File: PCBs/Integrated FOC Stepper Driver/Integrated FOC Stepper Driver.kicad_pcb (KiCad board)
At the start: 6 copper layers, 42 x 42 mm, 63 parts, among them J1 INPUT, J2 USB C Receptacle, J3 OUTPUT, J4 MOTOR, J5 Conn_01x02, SW1 BOOT, SW2 RESET, U1 PJ54M50SE, U2 PJ9500M33SA, U3 RP2040, U4 W25Q128JVS, U5 SN65HVD1050D, U6 MT6701CT, Y1 12MHz/12pF/50Ω/20ppm

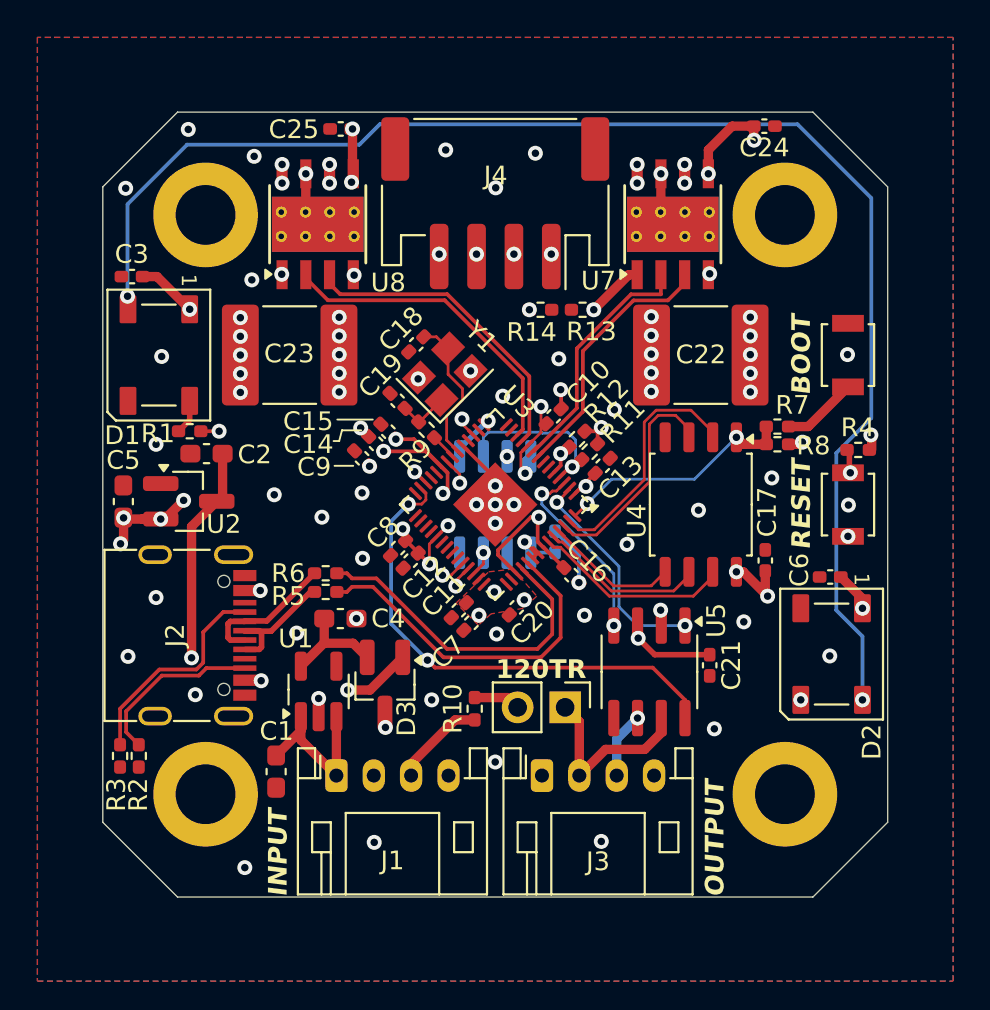
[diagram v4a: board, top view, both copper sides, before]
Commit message: Layout V2
Added a voltage divider from VBUS to measure up to 48V on ADC
Switch motor connector to JST-XH at 3A instead of 2A
Relayout to accomodate changes
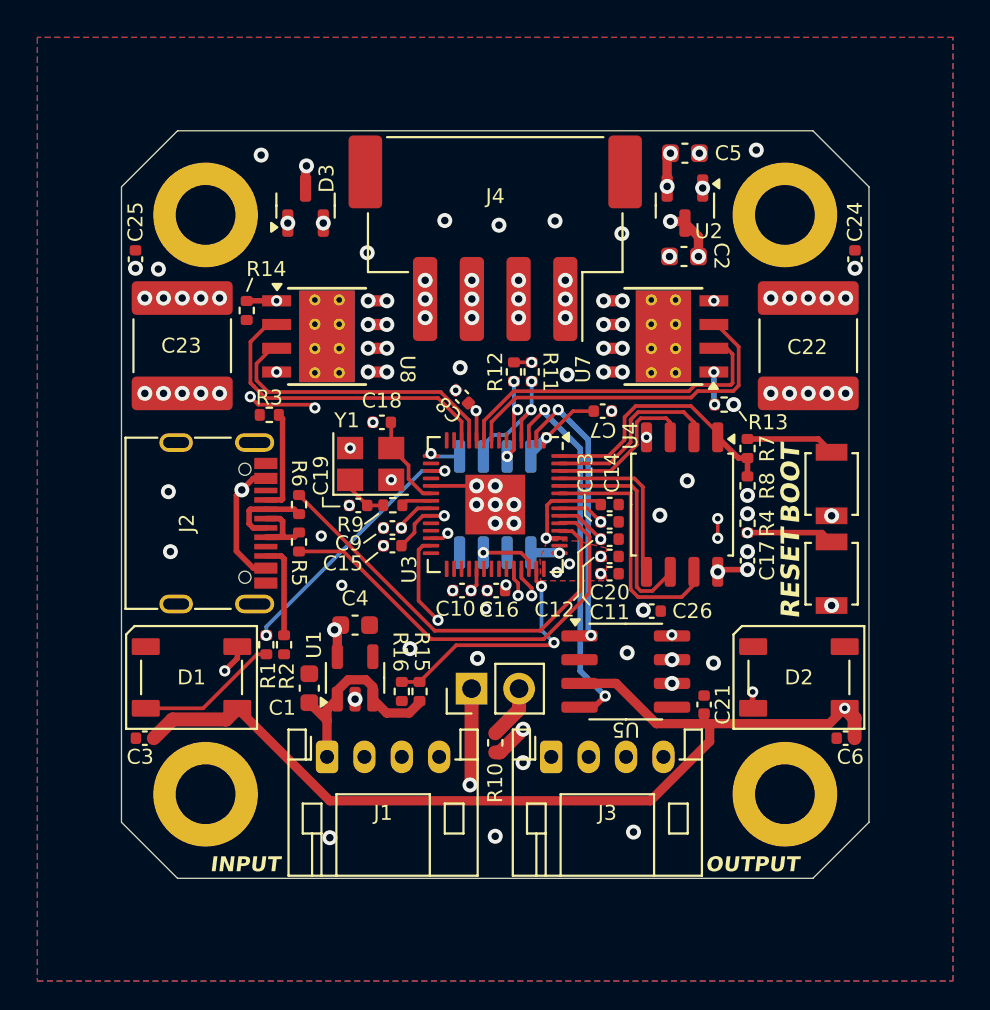
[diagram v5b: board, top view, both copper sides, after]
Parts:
- added R15: 150k, Resistor_SMD:R_0402_1005Metric, F.Cu at (46.0, 60.0)
- added R16: 10k, Resistor_SMD:R_0402_1005Metric, F.Cu at (45.0, 60.0)
- C1, C2, C4, C5: footprint Capacitor_SMD:C_0603_1608Metric_Pad1.08x0.95mm_HandSolder -> Capacitor_SMD:C_0603_1608Metric
- C10, C11, C12, C13, C14, C15, C16, C17, C18, C19, C20, C21, C24, C25, C3, C6, C7, C8, C9: footprint Capacitor_SMD:C_0402_1005Metric_Pad0.74x0.62mm_HandSolder -> Capacitor_SMD:C_0402_1005Metric
- C22, C23: footprint Capacitor_SMD:C_2220_5750Metric_Pad1.97x5.40mm_HandSolder -> Capacitor_SMD:C_2220_5750Metric
- C26: footprint Capacitor_SMD:C_0402_1005Metric_Pad0.74x0.62mm_HandSolder -> Capacitor_SMD:C_0402_1005Metric; moved to F.Cu
- D3, U2: footprint Package_TO_SOT_SMD:SOT-23_Handsoldering -> Package_TO_SOT_SMD:SOT-23
- J4: footprint Connector_JST:JST_PH_S4B-PH-SM4-TB_1x04-1MP_P2.00mm_Horizontal -> Connector_JST:JST_XH_S4B-XH-SM4-TB_1x04-1MP_P2.50mm_Horizontal
- R1, R10, R11, R12, R13, R14, R2, R3, R4, R5, R6, R7, R8, R9: footprint Resistor_SMD:R_0402_1005Metric_Pad0.72x0.64mm_HandSolder -> Resistor_SMD:R_0402_1005Metric
- U1: footprint Package_TO_SOT_SMD:SOT-23-5_HandSoldering -> Package_TO_SOT_SMD:SOT-23-5
- moved C5 35.4 mm to (60.1, 31.2), turned to 0 degrees
- moved U2 30.9 mm to (60.1, 34.0), turned to -90 degrees
- moved C2 27.6 mm to (60.1, 36.7)
- moved D3 26.0 mm to (39.9, 34.0), turned to 90 degrees
- moved C3 24.7 mm to (31.2, 62.5)
- moved R3 19.9 mm to (37.9, 45.2), turned to 180 degrees
- moved D1 17.3 mm to (33.8, 59.2), turned to 180 degrees
- moved R14 15.7 mm to (36.7, 39.6), turned to -90 degrees
- moved C7 13.3 mm to (55.8, 45.0), turned to 180 degrees
- moved C25 13.0 mm to (30.8, 36.9), turned to 90 degrees
- moved C14 12.9 mm to (56.1, 50.0), turned to 180 degrees
- moved R1 12.1 mm to (37.8, 57.5), turned to 90 degrees
- moved C12 10.7 mm to (56.1, 51.9), turned to 180 degrees
- moved C10 10.5 mm to (48.2, 54.6), turned to 0 degrees
- moved R2 9.79 mm to (38.7, 57.5)
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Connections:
- C3 pad 1: +3.3V -> +5V
- C6 pad 1: +3.3V -> +5V
- D1 pad 1: +3.3V -> +5V
- D2 pad 1: +3.3V -> +5V
- U3 pad 41: unconnected-(U3-GPIO29_ADC3-Pad41) -> /VBUS_MEASURE
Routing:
- net +5V: track 47.4 -> 132.2 mm, vias 3 -> 4
- net VBUS: track 53.2 -> 11.2 mm, vias 14 -> 16
- net Net-(D1-DOUT): track 77.0 -> 37.3 mm
- net +1V1: track 38.4 -> 19.2 mm, vias 4 -> 3
- net Net-(U1-VOUT): track 5.70 -> 24.4 mm, vias 0 -> 2
- net /CAN_H: track 21.7 -> 39.5 mm, vias 0 -> 2
- net /VBUS_MEASURE: track 0.00 -> 13.4 mm, vias 0 -> 2
- net +3.3V: track 34.8 -> 21.6 mm, vias 25 -> 21
- net /CAN_L: track 20.7 -> 33.5 mm, vias 1 -> 2
- net GND: track 13.1 -> 2.44 mm, vias 62 -> 65
- net /B2: track 28.4 -> 18.2 mm, vias 3 -> 5
- net /CAN_RX: track 10.2 -> 20.3 mm
- net /A1: track 25.8 -> 16.7 mm, vias 3 -> 5
- net /CAN_S: track 26.9 -> 17.8 mm
- net /B_CURRENT: track 36.4 -> 29.1 mm, vias 3 -> 4
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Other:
- board size 42 x 42 mm -> 40 x 40 mm
- board text removed: "120TR"
- board text removed: "DIFFERENTIAL"
- board text removed: "ROUTED"

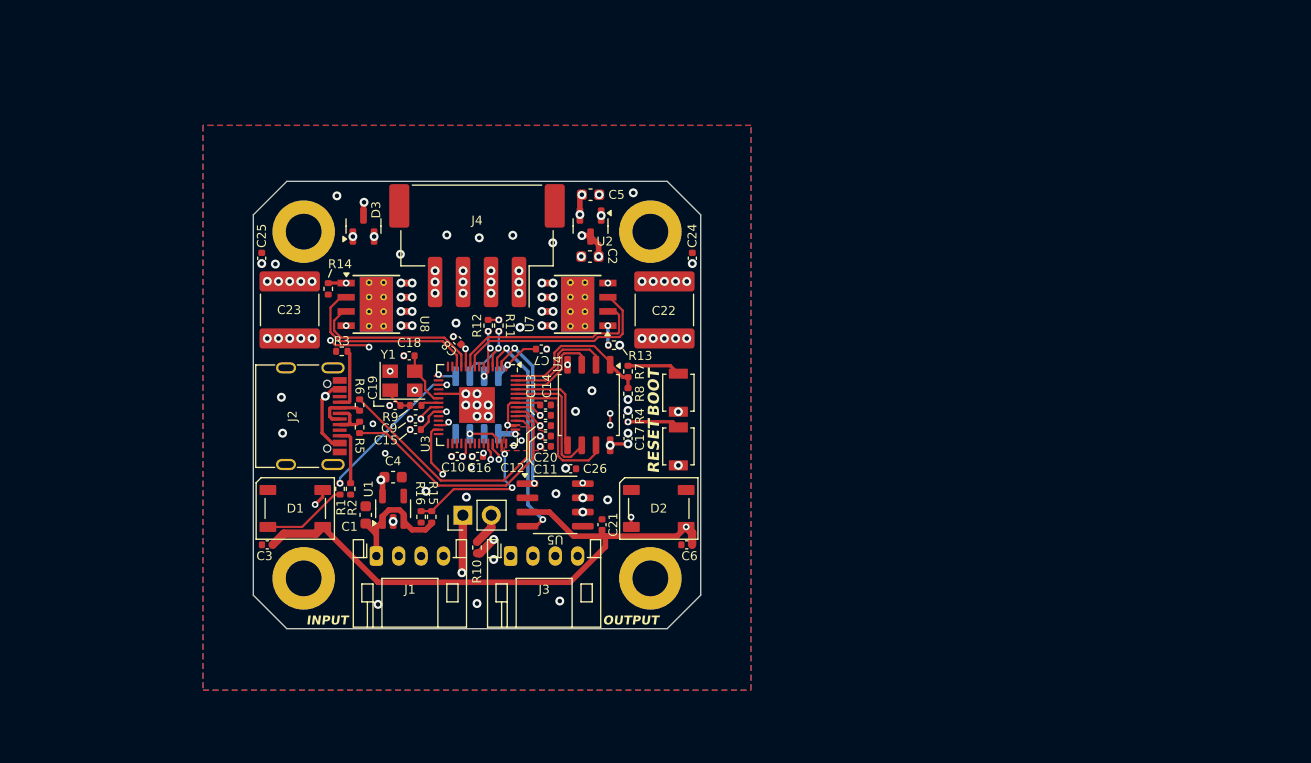
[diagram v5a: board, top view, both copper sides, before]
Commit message: Start re-layout with advice from John
6-layer stackup:
- Power
- Ground
- Signal
- Signal
- Ground
- Power

Switching to oscillator recommended by RPi in Hardware Design guide

Switching to THT JST-XH connector for motor to allow motor controllers to sit next to the connector

Fixed I2C pullup resistor values

Moved RP2040 decoupling caps to hierarchical sheet

Add SWD debug port
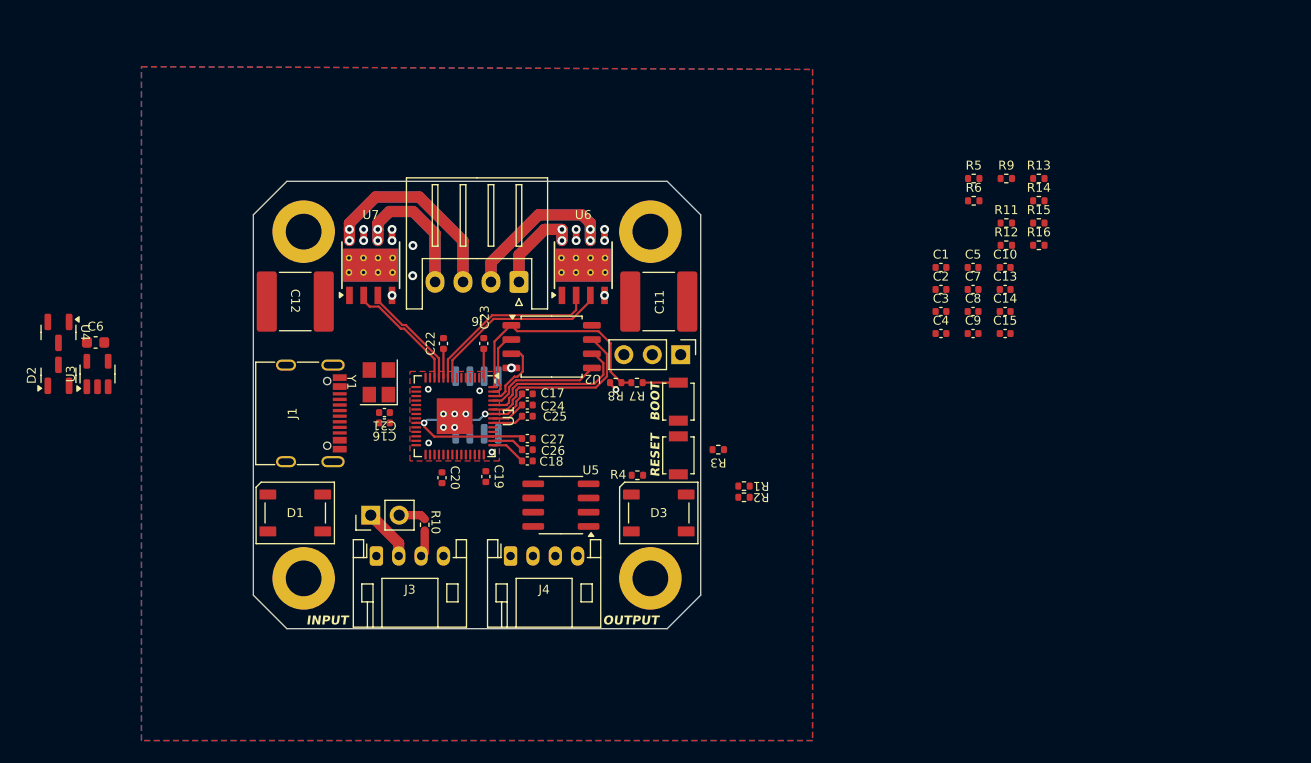
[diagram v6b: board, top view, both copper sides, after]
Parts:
- removed the C11 at (56.1, 52.8)
- removed the C12 at (56.1, 51.9)
- removed the D3 at (39.9, 34.0)
- removed the U1 at (42.5, 59.3)
- removed the U2 at (60.1, 34.0)
- added C22: 100nF, Capacitor_SMD:C_0402_1005Metric, F.Cu at (47.0, 44.5)
- added C23: 100nF, Capacitor_SMD:C_0402_1005Metric, F.Cu at (50.6, 44.5)
- added C27: 1uF, Capacitor_SMD:C_0402_1005Metric, F.Cu at (54.5, 53.0)
- added D2: BAT54C, Package_TO_SOT_SMD:SOT-23, F.Cu at (12.6, 47.3)
- added J2: Conn_01x03, Connector_PinHeader_2.54mm:PinHeader_1x03_P2.54mm_Vertical, F.Cu at (68.2, 45.5)
- added U3: PJ54M50SE, Package_TO_SOT_SMD:SOT-23-5, F.Cu at (16.1, 47.2)
- added U4: PJ9500M33SA, Package_TO_SOT_SMD:SOT-23, F.Cu at (12.6, 43.5)
- C1, C2: value 1uF -> 15pF; footprint Capacitor_SMD:C_0603_1608Metric -> Capacitor_SMD:C_0402_1005Metric
- C16, C20: value 1u -> 100nF
- C18, C19: value 22pF -> 100nF
- C26, C7: value 100nF -> 1uF
- C4: value 10uF -> 1uF; footprint Capacitor_SMD:C_0603_1608Metric -> Capacitor_SMD:C_0402_1005Metric
- C5: footprint Capacitor_SMD:C_0603_1608Metric -> Capacitor_SMD:C_0402_1005Metric
- C6: value 100nF -> 10uF; footprint Capacitor_SMD:C_0402_1005Metric -> Capacitor_SMD:C_0603_1608Metric
- J6: renamed from J4; footprint Connector_JST:JST_XH_S4B-XH-SM4-TB_1x04-1MP_P2.50mm_Horizontal -> Connector_JST:JST_XH_S4B-XH-A_1x04_P2.50mm_Horizontal
- R1: value 523 -> 27.4
- R11: value 5k -> 150k
- R12: value 5k -> 10k
- R15: value 150k -> 1.8k
- R16: value 10k -> 1.8k
- R2: value 5.1k -> 27.4
- R3: value 5.1k -> 1k
- R5, R6: value 27.4 -> 5.1k
- R9: value 1k -> 523
- SW1: renamed from SW2; value RESET -> ~
- SW2: renamed from SW1; value BOOT -> ~
- Y1: value 12MHz/12pF/50Ω/20ppm -> ABM8-272-T3
- moved R14 64.0 mm to (100.2, 31.7), turned to 0 degrees
- moved C3 63.7 mm to (91.5, 41.6), turned to 0 degrees
- moved R16 60.3 mm to (100.2, 35.7), turned to 0 degrees
- moved R15 60.3 mm to (100.2, 33.7), turned to 0 degrees
- moved R5 59.2 mm to (94.4, 29.8), turned to 0 degrees
- moved R6 57.9 mm to (94.4, 31.7), turned to 0 degrees
- moved R9 56.6 mm to (97.3, 29.8)
- moved C1 56.0 mm to (91.5, 37.7), turned to 0 degrees
- moved C6 55.9 mm to (15.9, 44.4), turned to 0 degrees
- moved C15 53.4 mm to (97.2, 43.6)
- moved C10 51.8 mm to (97.2, 37.7)
- moved C4 50.6 mm to (91.5, 43.6)
- moved C9 50.4 mm to (94.3, 43.6)
- moved R12 46.9 mm to (97.3, 35.7), turned to 0 degrees
- moved R11 46.3 mm to (97.3, 33.7), turned to 0 degrees
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- renumbered C22 to C11, C23 to C12, D2 to D3, J2 to J1, J1 to J3, J3 to J4, U3 to U1, U4 to U2, U7 to U6, U8 to U7, U6 to U8
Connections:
- C1 pad 1: VBUS -> Net-(U1-XIN)
- C10 pad 1: GND -> +5V
- C10 pad 2: +3.3V -> GND
- C13 pad 1: GND -> VBUS
- C13 pad 2: +3.3V -> GND
- C14 pad 1: GND -> VBUS
- C14 pad 2: +1V1 -> GND
- C15 pad 1: GND -> +3.3V
- C15 pad 2: +1V1 -> GND
- C16 pad 1: GND -> +1V1
- C16 pad 2: +1V1 -> GND
- C17 pad 1: +3.3V -> +1V1
- C18 pad 1: GND -> +3.3V
- C18 pad 2: /XIN -> GND
- C19 pad 1: GND -> +3.3V
- C19 pad 2: Net-(C19-Pad2) -> GND
- C2 pad 1: +5V -> GND
- C2 pad 2: GND -> Net-(C2-Pad2)
- C21 pad 1: +5V -> +3.3V
- C24 pad 1: VBUS -> +3.3V
- C25 pad 1: VBUS -> +3.3V
- C3 pad 1: +5V -> +3.3V
- C4 pad 1: Net-(U1-VOUT) -> VBUS
- C5 pad 1: +3.3V -> +5V
- C6 pad 1: +5V -> Net-(U3-VOUT)
- C7 pad 1: GND -> +3.3V
- C7 pad 2: +3.3V -> GND
- C8 pad 1: GND -> +5V
- C8 pad 2: +3.3V -> GND
- C9 pad 1: GND -> +5V
- C9 pad 2: +3.3V -> GND
- J1 pad A5: Net-(J2-CC1) -> Net-(J1-CC1)
- J1 pad B5: Net-(J2-CC2) -> Net-(J1-CC2)
- R1 pad 1: Net-(D1-DIN) -> /USB_D+
- R1 pad 2: /NEOPIXEL -> /USB_DP
- R11 pad 1: /SDA -> VBUS
- R11 pad 2: +3.3V -> /VBUS_MEASURE
- R12 pad 1: /SCL -> /VBUS_MEASURE
- R12 pad 2: +3.3V -> GND
- R15 pad 1: VBUS -> /SDA
- R15 pad 2: /VBUS_MEASURE -> +3.3V
- R16 pad 1: /VBUS_MEASURE -> /SCL
- R16 pad 2: GND -> +3.3V
- R2 pad 1: Net-(J2-CC2) -> /USB_DN
- R2 pad 2: GND -> /USB_D-
- R3 pad 1: Net-(J2-CC1) -> Net-(C2-Pad2)
- R3 pad 2: GND -> Net-(U1-XOUT)
- R4 pad 2: /RUN -> Net-(U1-RUN)
- R5 pad 1: /USB_D+ -> Net-(J1-CC1)
- R5 pad 2: /USB_DP -> GND
- R6 pad 1: /USB_DN -> Net-(J1-CC2)
- R6 pad 2: /USB_D- -> GND
- R9 pad 1: Net-(C19-Pad2) -> Net-(D1-DIN)
- R9 pad 2: /XOUT -> /NEOPIXEL
- SW1 pad 1: GND -> Net-(U1-RUN)
- SW1 pad 2: /RUN -> GND
- U1 pad 20: /XIN -> Net-(U1-XIN)
- U1 pad 21: /XOUT -> Net-(U1-XOUT)
- U1 pad 24: unconnected-(U3-SWCLK-Pad24) -> Net-(J2-Pin_1)
- U1 pad 25: unconnected-(U3-SWD-Pad25) -> Net-(J2-Pin_2)
- U1 pad 26: /RUN -> Net-(U1-RUN)
- Y1 pad 1: Net-(C19-Pad2) -> Net-(C2-Pad2)
- Y1 pad 3: /XIN -> Net-(U1-XIN)
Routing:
- net +5V: track 132.2 -> 0.00 mm, vias 4 -> 0
- net Net-(D1-DOUT): track 37.3 -> 0.00 mm, vias 2 -> 0
- net /B_CURRENT: track 29.1 -> 0.00 mm, vias 4 -> 0
- net Net-(U1-VOUT): track 24.4 -> 0.00 mm, vias 2 -> 0
- net /USB_DP: track 23.5 -> 0.00 mm
- net /RUN: track 23.1 -> 0.00 mm, vias 2 -> 0
- net /USB_DN: track 23.0 -> 0.00 mm
- net /A_CURRENT: track 23.0 -> 0.00 mm, vias 5 -> 0
- net /VUSB: track 22.4 -> 0.00 mm, vias 2 -> 0
- net /CAN_H: track 39.5 -> 18.2 mm, vias 2 -> 0
- net /CAN_RX: track 20.3 -> 0.00 mm, vias 2 -> 0
- net /CAN_S: track 17.8 -> 0.00 mm, vias 2 -> 0
- net /B2: track 18.2 -> 36.0 mm, vias 5 -> 2
- net /CAN_L: track 33.5 -> 15.8 mm, vias 2 -> 0
- net /CAN_TX: track 15.6 -> 0.00 mm, vias 2 -> 0
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- added copper zone on In2.Cu, net +3.3V
- added copper zone on In1.Cu, net GND
- added copper zone on In3.Cu, net GND
- added copper zone on B.Cu, net VBUS
- added copper zone on F.Cu, net VBUS
- removed copper zone on In1.Cu, net +3.3V
- removed copper zone on B.Cu, net GND
- removed copper zone on F.Cu, net GND
- removed copper zone on In2.Cu, net GND
- removed copper zone on In3.Cu, net VBUS
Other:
- board text added: "A1"
- board text added: "A2"
- board text added: "B1"
- board text added: "B2"
- board text added: "BOOT"
- board text added: "RESET"

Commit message: Finish new layout
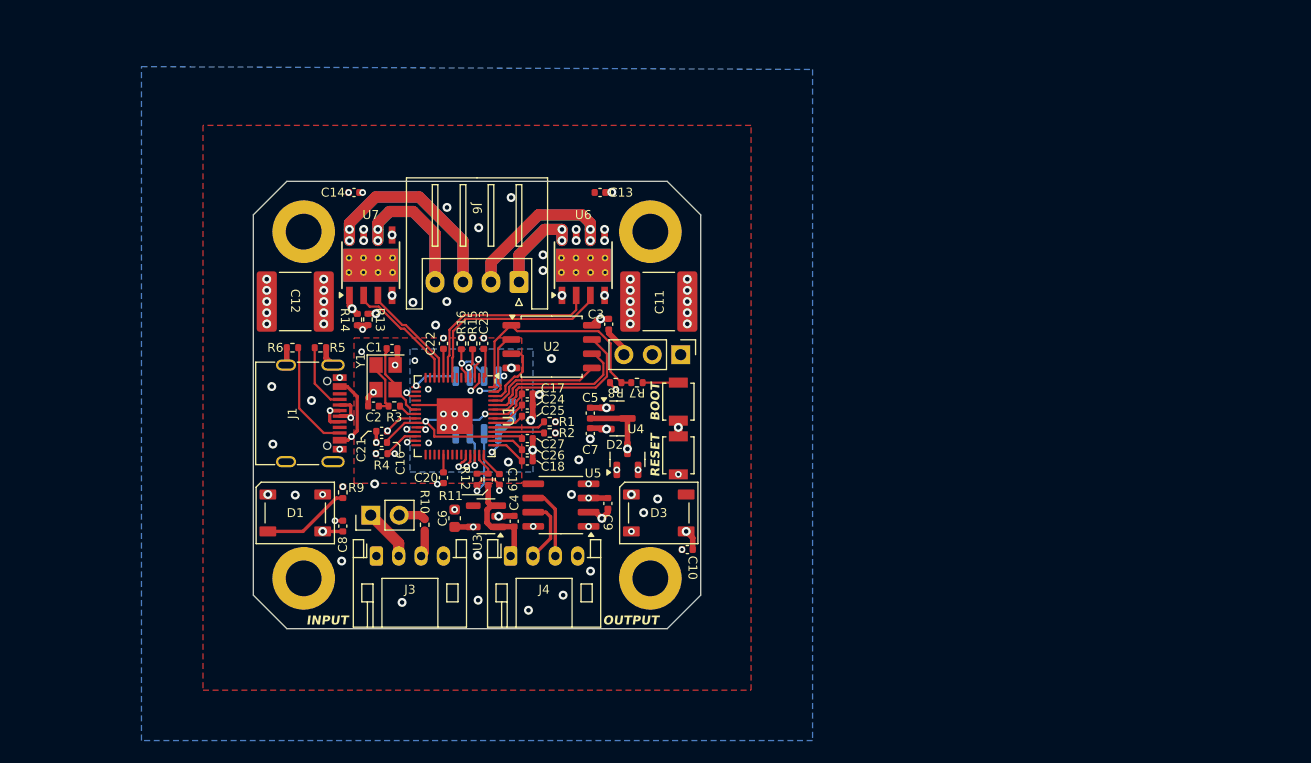
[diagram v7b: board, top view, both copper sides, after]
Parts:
- C15: moved to B.Cu
- SW1, SW2: value ~ -> BTN
- moved R9 65.6 mm to (38.0, 57.8), turned to 90 degrees
- moved R6 62.3 mm to (33.5, 44.9), turned to 180 degrees
- moved R14 61.8 mm to (39.3, 42.4), turned to -90 degrees
- moved R13 61.3 mm to (40.2, 42.4), turned to -90 degrees
- moved R5 60.3 mm to (36.0, 44.9)
- moved C8 59.5 mm to (38.0, 60.8), turned to 90 degrees
- moved C14 59.2 mm to (39.0, 31.0), turned to 180 degrees
- moved R16 52.4 mm to (48.6, 44.5), turned to 90 degrees
- moved C2 51.8 mm to (40.7, 50.1)
- moved R15 51.8 mm to (49.6, 44.5), turned to 90 degrees
- moved R12 51.7 mm to (50.0, 56.6), turned to -90 degrees
- moved R11 51.7 mm to (51.0, 56.6), turned to 90 degrees
- moved D2 51.4 mm to (63.5, 54.9)
- moved U4 50.5 mm to (62.5, 51.2), turned to 0 degrees
- moved C1 49.6 mm to (42.4, 45.0)
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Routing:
- net VBUS: track 0.00 -> 71.4 mm, vias 6 -> 19
- net +5V: track 0.00 -> 60.7 mm, vias 0 -> 4
- net GND: track 0.00 -> 38.8 mm, vias 10 -> 69
- net /A_CURRENT: track 0.00 -> 37.2 mm, vias 0 -> 3
- net /VUSB: track 0.00 -> 32.6 mm, vias 0 -> 2
- net Net-(U1-RUN): track 0.00 -> 32.3 mm, vias 0 -> 2
- net Net-(J2-Pin_2): track 0.00 -> 29.5 mm, vias 0 -> 1
- net Net-(D1-DOUT): track 0.00 -> 29.1 mm, vias 0 -> 2
- net Net-(J2-Pin_1): track 0.00 -> 27.7 mm, vias 0 -> 1
- net /USB_D+: track 0.00 -> 24.8 mm, vias 0 -> 2
- net /USB_D-: track 0.00 -> 23.8 mm, vias 0 -> 2
- net /B_CURRENT: track 0.00 -> 23.6 mm, vias 0 -> 2
- net /CAN_TX: track 0.00 -> 19.3 mm, vias 0 -> 2
- net /CAN_RX: track 0.00 -> 19.0 mm, vias 0 -> 2
- net /NEOPIXEL: track 0.00 -> 18.8 mm, vias 0 -> 2
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- added copper zone on B.Cu, net GND
- added copper zone on F.Cu, net GND
- removed copper zone on F.Cu, net VBUS

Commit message: Small updates to layout
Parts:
- moved C3 0.10 mm to (61.9, 42.8)
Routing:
- net VBUS: track 71.4 -> 99.5 mm
- net GND: track 38.8 -> 39.0 mm, vias 69 -> 72
- net +3.3V: vias 14 -> 16
